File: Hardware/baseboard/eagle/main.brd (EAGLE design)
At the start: 108.5 x 120.5 mm, 176 parts, among them J1 MICROUSB-FEM, X1 JST-4POS-2X4POS, X1.2 TACH/LAP, X2.2 VRAILS+, X2.3 5V+SoC

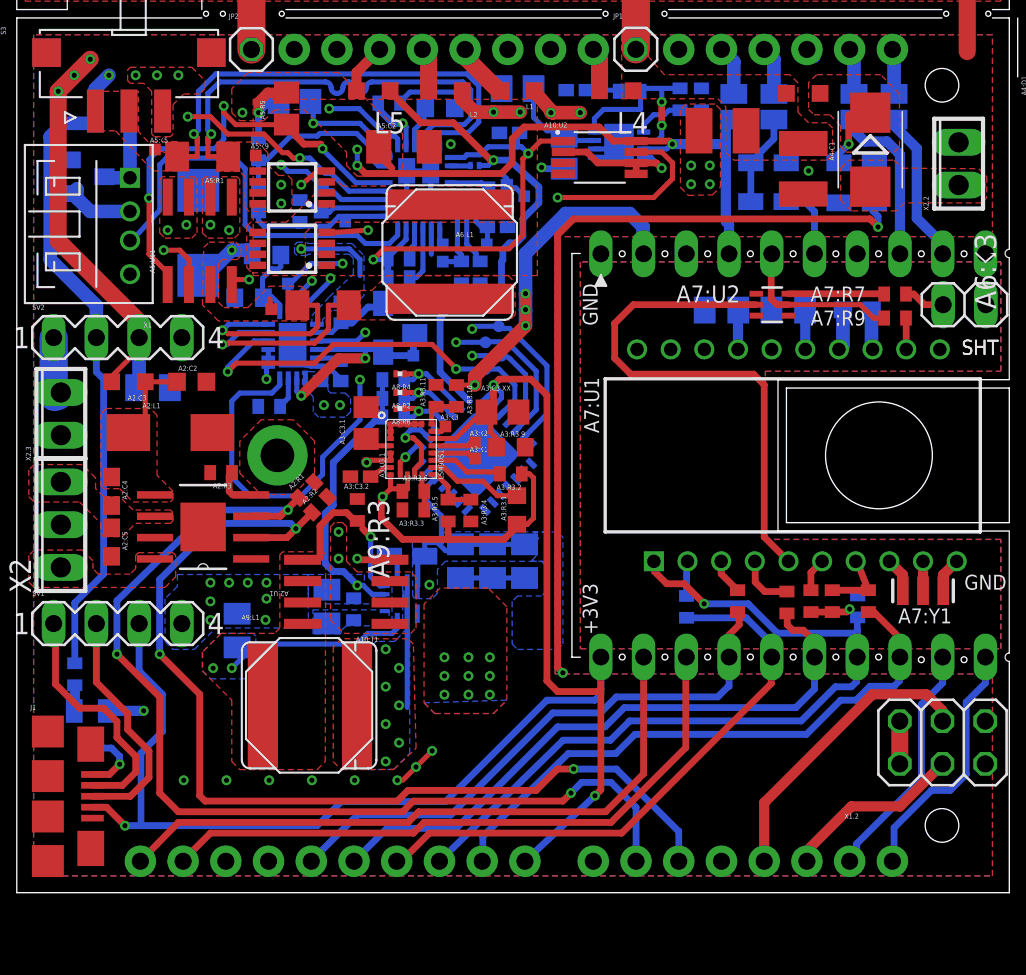
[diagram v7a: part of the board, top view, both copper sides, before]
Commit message: baseboard: 1 airwire left -> swap motor terminal with 5V
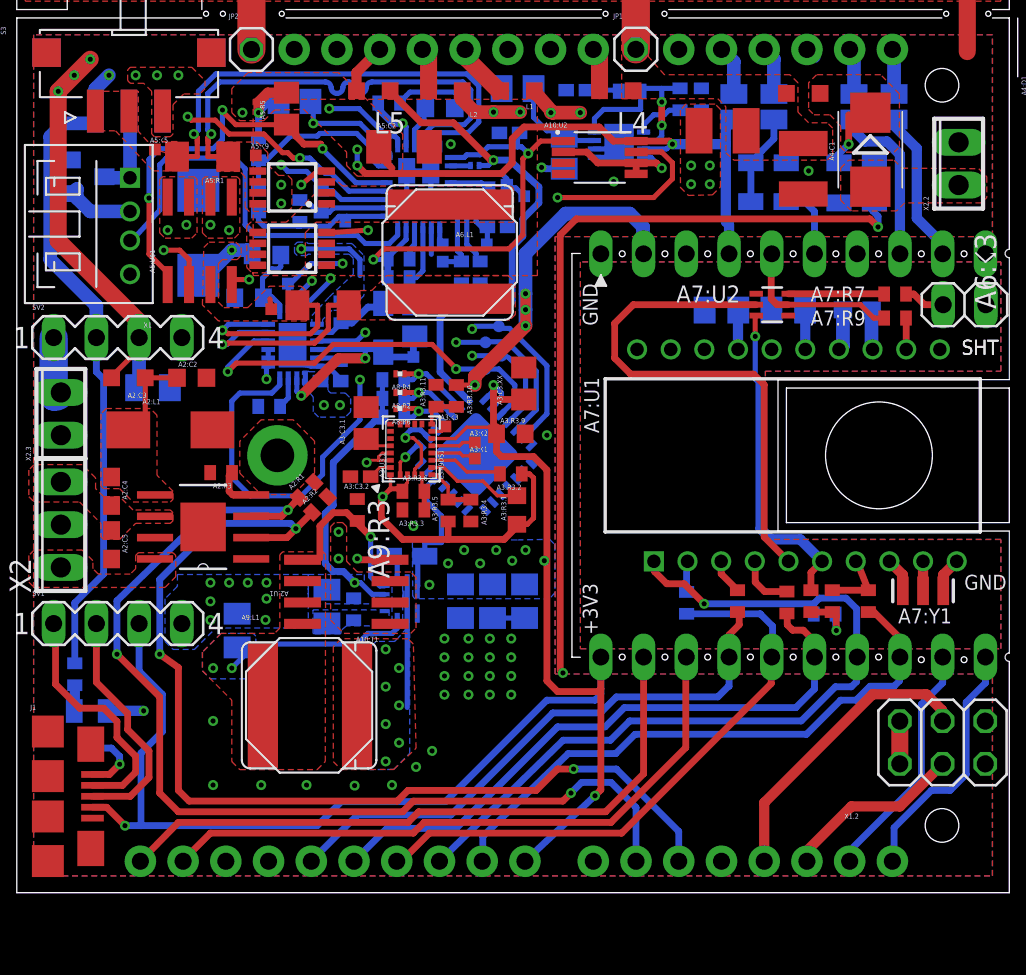
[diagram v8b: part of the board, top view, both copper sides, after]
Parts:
- moved A9:C2 2.38 mm to (31.4, 36.3)
- moved A9:C3 2.38 mm to (33.3, 36.3)
- moved A9:C4 2.38 mm to (35.2, 36.3)
- moved A3:C3.XX 2.12 mm to (35.1, 49.3), turned to 90 degrees
- moved A7:R1 2.02 mm to (53.0, 35.6), turned to 0 degrees
- moved A3:R3.9 0.79 mm to (34.4, 46.3)
- moved A2:C2 0.24 mm to (15.4, 49.6)
- moved A2:L1 0.24 mm to (11.6, 49.6)
- moved A7:R2 0.24 mm to (44.8, 36.2)
- moved A2:C3 0.16 mm to (14.1, 46.5)
- moved A2:C5 0.16 mm to (10.6, 39.7)
- moved A6:C2 0.08 mm to (28.7, 53.0)
- moved A6:☇5 0.08 mm to (28.6, 50.8)
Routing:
- net A7:RST: track 1.99 -> 19.3 mm, vias 0 -> 1
- net +5V: track 83.9 -> 76.4 mm, vias 5 -> 12
- net GND: track 31.9 -> 24.8 mm, vias 28 -> 38
- net SYSTWI.!INT: track 100.0 -> 96.6 mm
- net TOP.!RST: track 66.2 -> 68.8 mm
- net A10.!ACT: track 44.9 -> 42.9 mm
- net +3V3: track 72.5 -> 74.0 mm
- net MISO: track 34.8 -> 35.5 mm
- net !CS0: track 47.3 -> 48.0 mm
- net PWR.MOTA: track 60.4 -> 61.1 mm
- net TOP.VSYS/GUARD: track 21.3 -> 21.9 mm
- net A5:CSN: track 27.2 -> 26.6 mm
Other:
- board text removed: "+5V"
